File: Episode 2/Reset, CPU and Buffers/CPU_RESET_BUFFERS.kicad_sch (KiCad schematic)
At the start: 27 parts, among them SW1 RST SW, U1 74AHCT541, U2 74HC245, U3 HD63C09P, U4 74AHCT541, U5 74AHCT244, U6 MIC1232

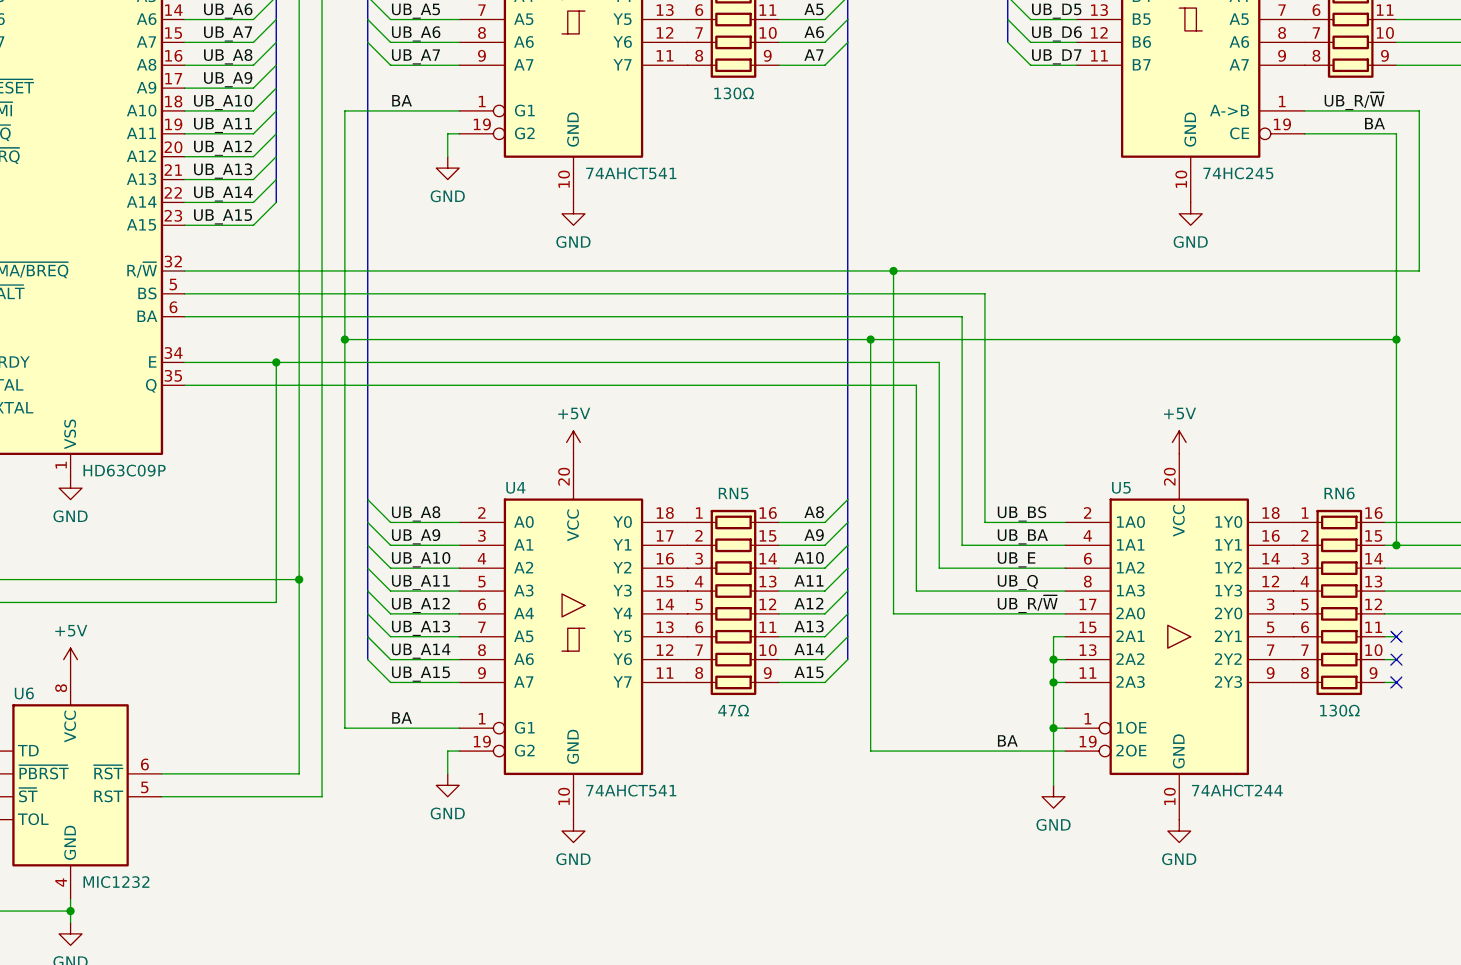
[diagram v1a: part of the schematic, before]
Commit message: Added resistor to MIC1232
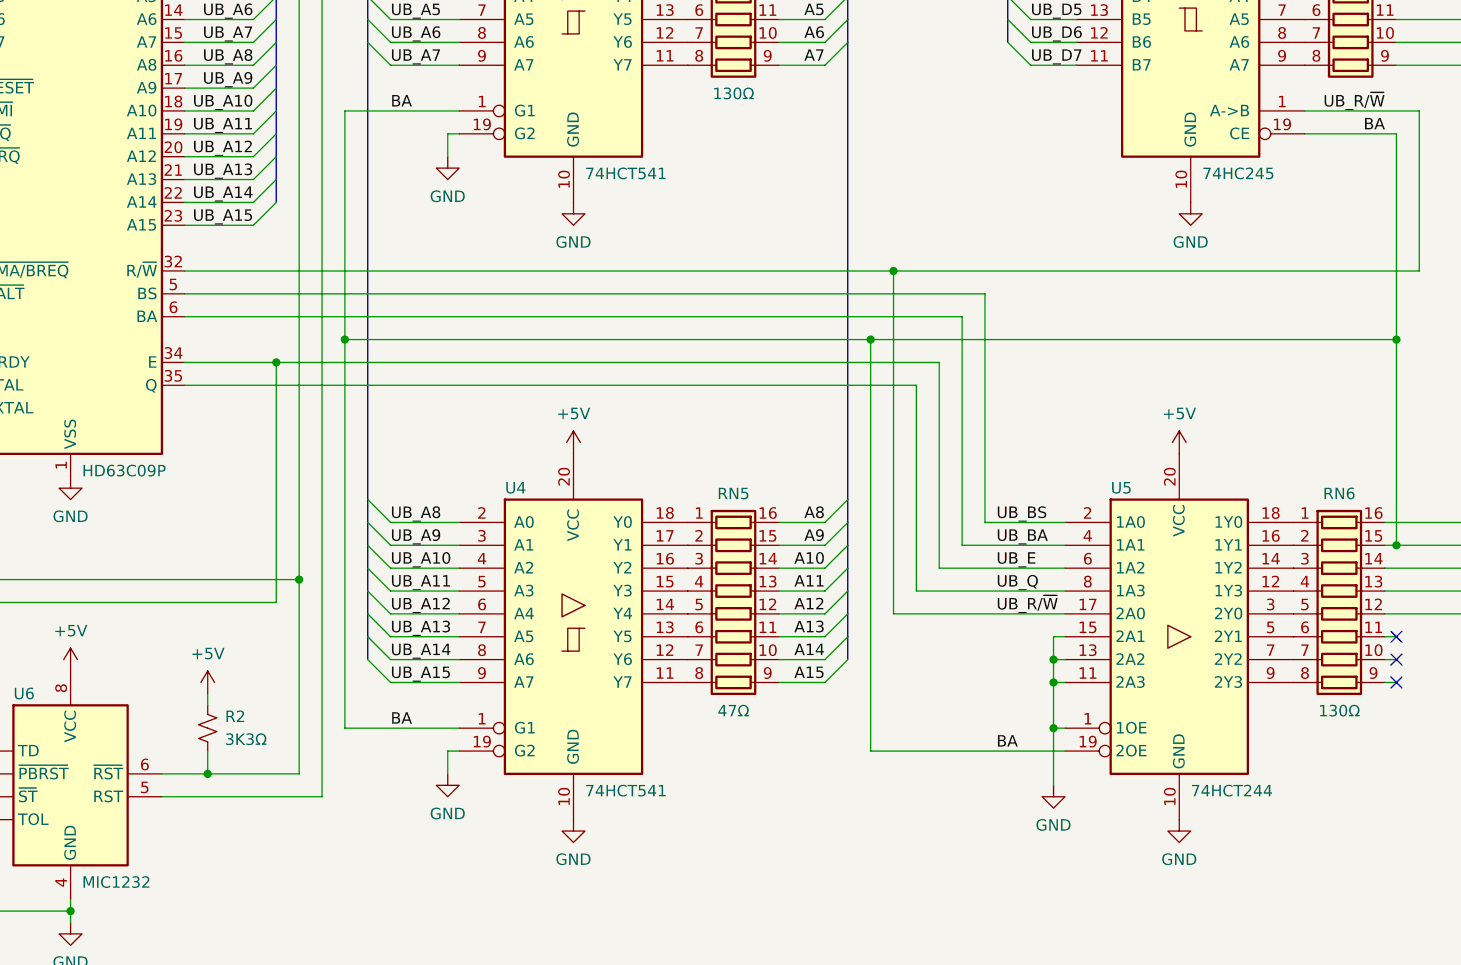
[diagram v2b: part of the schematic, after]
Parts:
- added R2: 3K3Ω, symbol Device:R_Small_US
- U1, U4: value 74AHCT541 -> 74HCT541
- U5: value 74AHCT244 -> 74HCT244
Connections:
- net +5V: now also R2.1
- net ~{RESET}: now also R2.2
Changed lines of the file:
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@@
 	)
 	(junction
+		(at 93.98 144.78)
+		(diameter 0)
+		(color 0 0 0 0)
+	)
+	(junction
 		(at 124.46 196.85)
 		(diameter 0)
@@
 	(wire
 		(pts
-			(xy 88.9 144.78) (xy 104.14 144.78)
+			(xy 88.9 144.78) (xy 93.98 144.78)
 		)
 		(stroke
@@
 	(wire
 		(pts
+			(xy 93.98 144.78) (xy 104.14 144.78)
+		)
+		(stroke
+			(width 0)
+			(type default)
+		)
+	)
+	(wire
+		(pts
 			(xy 226.06 63.5) (xy 237.49 63.5)
 		)
@@
 	(wire
 		(pts
+			(xy 93.98 135.89) (xy 93.98 137.16)
+		)
+		(stroke
+			(width 0)
+			(type default)
+		)
+	)
+	(wire
+		(pts
 			(xy 177.8 93.98) (xy 177.8 119.38)
 		)
@@
 		)
 	)
+	(wire
+		(pts
+			(xy 93.98 142.24) (xy 93.98 144.78)
+		)
+		(stroke
+			(width 0)
+			(type default)
+		)
+	)
 	(bus
 		(pts
@@
 	)
 	(symbol
+		(lib_id "power:+5V")
+		(at 93.98 135.89 0)
+		(unit 1)
+		(exclude_from_sim no)
+		(in_bom yes)
+		(on_board yes)
+		(dnp no)
+		(property "Reference" "#PWR027"
+			(at 93.98 139.7 0)
+			(effects
+				(font
+					(size 1.27 1.27)
+				)
+				(hide yes)
+			)
+		)
+		(property "Value" "+5V"
+			(at 93.98 131.445 0)
+			(effects
+				(font
+					(size 1.27 1.27)
+				)
+			)
+		)
+		(property "Footprint" ""
+			(at 93.98 135.89 0)
+			(effects
+				(font
+					(size 1.27 1.27)
+				)
+				(hide yes)
+			)
+		)
+		(property "Datasheet" ""
+			(at 93.98 135.89 0)
+			(effects
+				(font
+					(size 1.27 1.27)
+				)
+				(hide yes)
+			)
+		)
+		(property "Description" "Power symbol creates a global label with name \"+5V\""
+			(at 93.98 135.89 0)
+			(effects
+				(font
+					(size 1.27 1.27)
+				)
+				(hide yes)
+			)
+		)
+		(pin "1"
+		)
+		(instances
+			(project "Reset, CPU and Buffers"
+				(path "/2180879c-3df6-4382-a01a-a65e59e9c299/154d3636-9585-43f9-bdff-90ca5096544f"
+					(reference "#PWR027")
+					(unit 1)
+				)
+			)
+		)
+	)
+	(symbol
 		(lib_id "power:GND")
 		(at 134.62 81.28 0)
@@
 			)
 		)
-		(property "Value" "74AHCT244"
+		(property "Value" "74HCT244"
 			(at 203.2 146.685 0)
 			(effects
@@
 			)
 		)
-		(property "Value" "74AHCT541"
+		(property "Value" "74HCT541"
 			(at 135.89 146.685 0)
 			(effects
@@
 			)
 		)
-		(property "Value" "74AHCT541"
+		(property "Value" "74HCT541"
 			(at 135.89 78.105 0)
 			(effects
@@
 					(unit 1)
 				)
+			)
+		)
+	)
+	(symbol
+		(lib_id "Device:R_Small_US")
+		(at 93.98 139.7 0)
+		(unit 1)
+		(exclude_from_sim no)
+		(in_bom yes)
+		(on_board yes)
+		(dnp no)
+		(property "Reference" "R2"
+			(at 95.885 138.43 0)
+			(effects
+				(font
+					(size 1.27 1.27)
+				)
+				(justify left)
+			)
+		)
+		(property "Value" "3K3Ω"
+			(at 95.885 140.97 0)
+			(effects
+				(font
+					(size 1.27 1.27)
+				)
+				(justify left)
+			)
+		)
+		(property "Footprint" ""
+			(at 93.98 139.7 0)
+			(effects
+				(font
+					(size 1.27 1.27)
+				)
+				(hide yes)
+			)
+		)
+		(property "Datasheet" "~"
+			(at 93.98 139.7 0)
+			(effects
+				(font
+					(size 1.27 1.27)
+				)
+				(hide yes)
+			)
+		)
+		(property "Description" "Resistor, small US symbol"
+			(at 93.98 139.7 0)
+			(effects
+				(font
+					(size 1.27 1.27)
+				)
+				(hide yes)
+			)
+		)
+		(pin "2"
+		)
+		(pin "1"
+		)
+		(instances
+			(project "Reset, CPU and Buffers"
+				(path "/2180879c-3df6-4382-a01a-a65e59e9c299/154d3636-9585-43f9-bdff-90ca5096544f"
+					(reference "R2")
+					(unit 1)
+				)
